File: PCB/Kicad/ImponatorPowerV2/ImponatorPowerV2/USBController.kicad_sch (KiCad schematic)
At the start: 17 parts, among them J3 Conn_01x04_Pin, U1 STUSB4500QTR

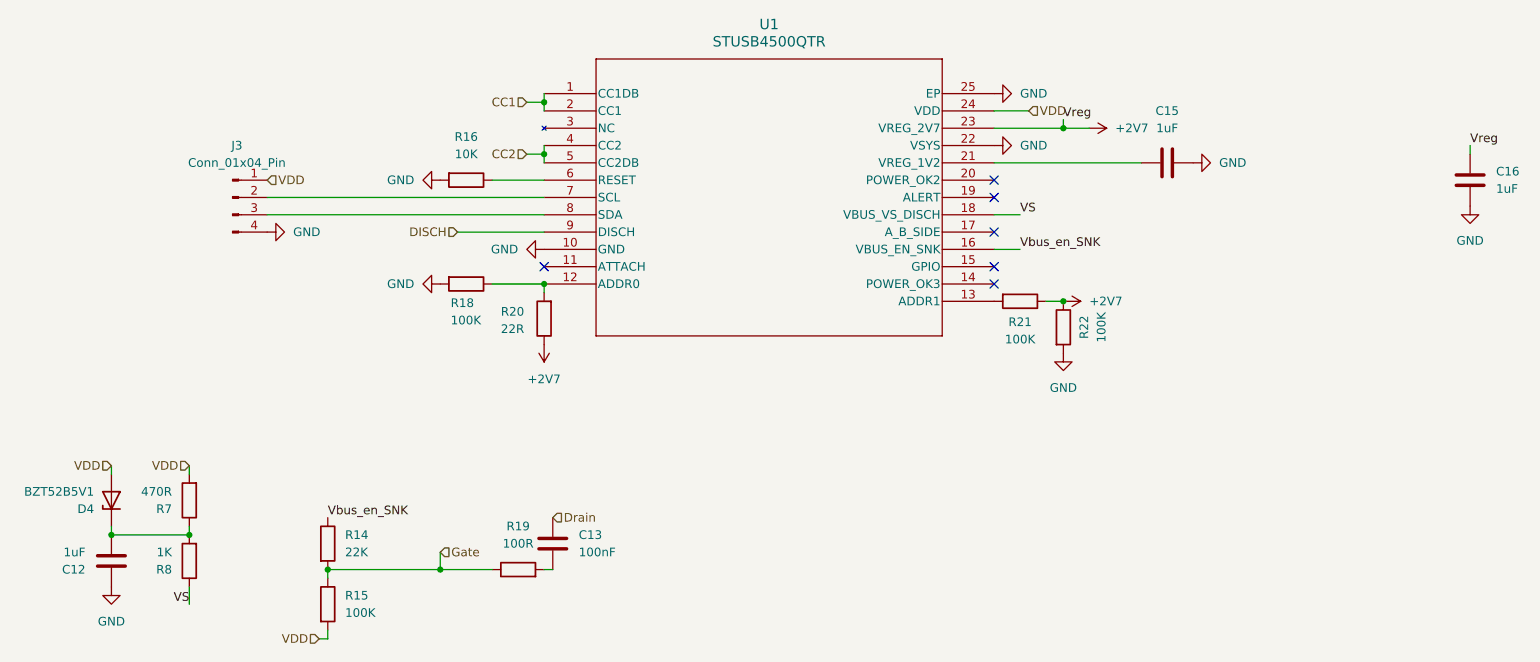
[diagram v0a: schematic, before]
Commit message: PCB routed, not ready for production
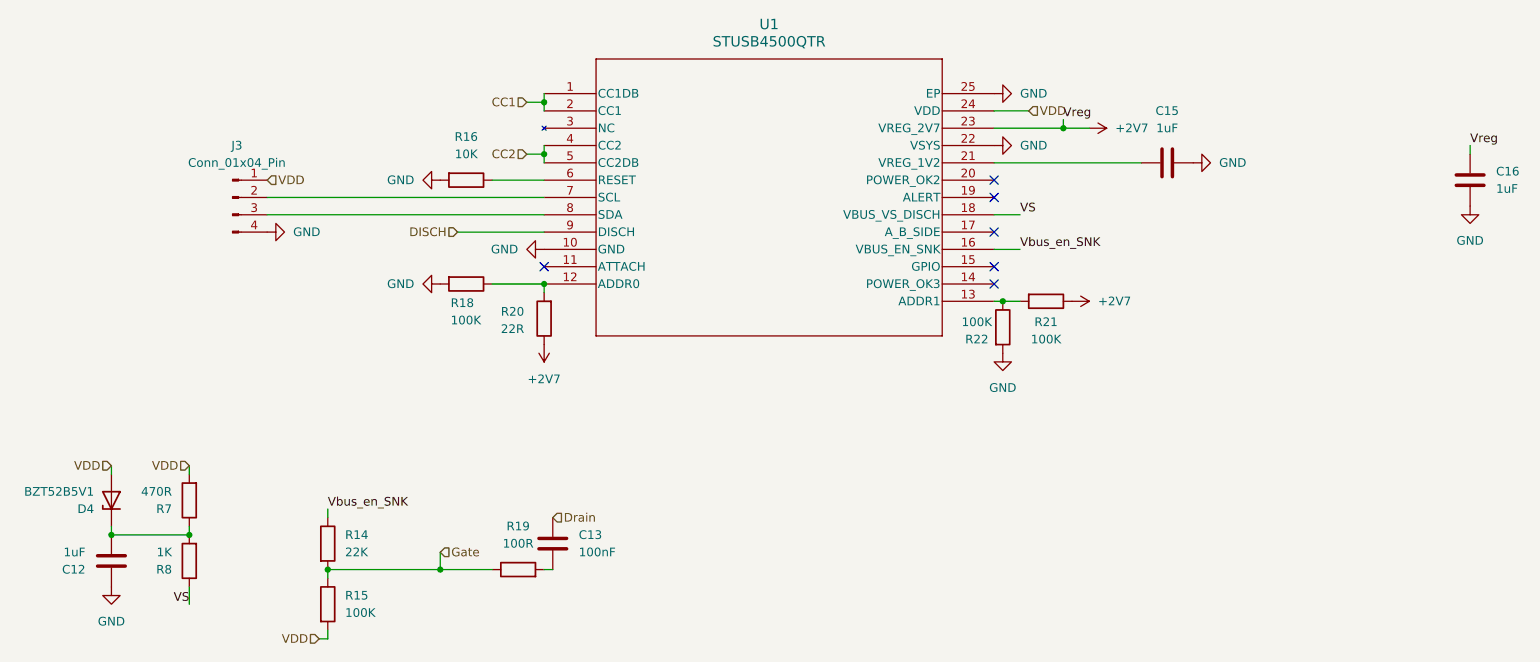
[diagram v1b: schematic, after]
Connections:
- net +2V7: no longer R22.1
- net at R21.2, U1.13 (ADDR1): now also R22.1
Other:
- moved on the sheet: R21, R22
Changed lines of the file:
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@@
 	(paper "A4")
-	(junction
-		(at 179.07 104.14)
-		(diameter 0)
-		(color 0 0 0 0)
-	)
 	(junction
 		(at 102.87 82.55)
@@
 	)
 	(junction
+		(at 170.18 104.14)
+		(diameter 0)
+		(color 0 0 0 0)
+	)
+	(junction
 		(at 102.87 101.6)
 		(diameter 0)
@@
 	(wire
 		(pts
-			(xy 176.53 104.14) (xy 179.07 104.14)
-		)
-		(stroke
-			(width 0)
-			(type default)
-		)
-	)
-	(wire
-		(pts
 			(xy 172.72 96.52) (xy 168.91 96.52)
 		)
@@
 	(wire
 		(pts
+			(xy 71.12 134.62) (xy 71.12 135.89)
+		)
+		(stroke
+			(width 0)
+			(type default)
+		)
+	)
+	(wire
+		(pts
 			(xy 87.63 143.51) (xy 95.25 143.51)
 		)
@@
 	(wire
 		(pts
+			(xy 170.18 104.14) (xy 172.72 104.14)
+		)
+		(stroke
+			(width 0)
+			(type default)
+		)
+	)
+	(wire
+		(pts
 			(xy 102.87 73.66) (xy 102.87 74.93)
 		)
@@
 		(pts
 			(xy 190.5 83.82) (xy 168.91 83.82)
+		)
+		(stroke
+			(width 0)
+			(type default)
+		)
+	)
+	(wire
+		(pts
+			(xy 168.91 104.14) (xy 170.18 104.14)
 		)
 		(stroke
@@
 	)
 	(label "Vbus_en_SNK"
-		(at 71.12 135.89 0)
+		(at 71.12 134.62 0)
 		(effects
 			(font
@@
 	(symbol
 		(lib_id "power:GND")
-		(at 179.07 111.76 0)
+		(at 170.18 111.76 0)
 		(unit 1)
 		(exclude_from_sim no)
@@
 		(fields_autoplaced yes)
 		(property "Reference" "#PWR039"
-			(at 179.07 118.11 0)
+			(at 170.18 118.11 0)
 			(effects
 				(font
@@
 		)
 		(property "Value" "GND"
-			(at 179.07 116.84 0)
+			(at 170.18 116.84 0)
 			(effects
 				(font
@@
 		)
 		(property "Footprint" ""
-			(at 179.07 111.76 0)
+			(at 170.18 111.76 0)
 			(effects
 				(font
@@
 		)
 		(property "Datasheet" ""
-			(at 179.07 111.76 0)
+			(at 170.18 111.76 0)
 			(effects
 				(font
@@
 		)
 		(property "Description" "Power symbol creates a global label with name \"GND\" , ground"
-			(at 179.07 111.76 0)
+			(at 170.18 111.76 0)
 			(effects
 				(font
@@
 	(symbol
 		(lib_id "Device:R")
-		(at 179.07 107.95 0)
+		(at 170.18 107.95 0)
 		(unit 1)
 		(exclude_from_sim no)
@@
 		(dnp no)
 		(property "Reference" "R22"
-			(at 182.118 107.95 90)
+			(at 166.37 109.728 0)
 			(effects
 				(font
@@
 		)
 		(property "Value" "100K"
-			(at 184.658 107.95 90)
+			(at 166.37 107.188 0)
 			(effects
 				(font
@@
 		)
 		(property "Footprint" "Resistor_SMD:R_0603_1608Metric"
-			(at 177.292 107.95 90)
+			(at 168.402 107.95 90)
 			(effects
 				(font
@@
 		)
 		(property "Datasheet" "~"
-			(at 179.07 107.95 0)
+			(at 170.18 107.95 0)
 			(effects
 				(font
@@
 		)
 		(property "Description" "Resistor"
-			(at 179.07 107.95 0)
+			(at 170.18 107.95 0)
 			(effects
 				(font
@@
 	(symbol
 		(lib_id "Device:R")
-		(at 172.72 104.14 270)
+		(at 176.53 104.14 270)
 		(unit 1)
 		(exclude_from_sim no)
@@
 		(dnp no)
 		(property "Reference" "R21"
-			(at 172.72 107.188 90)
+			(at 176.53 107.188 90)
 			(effects
 				(font
@@
 		)
 		(property "Value" "100K"
-			(at 172.72 109.728 90)
+			(at 176.53 109.728 90)
 			(effects
 				(font
@@
 		)
 		(property "Footprint" "Resistor_SMD:R_0603_1608Metric"
-			(at 172.72 102.362 90)
+			(at 176.53 102.362 90)
 			(effects
 				(font
@@
 		)
 		(property "Datasheet" "~"
-			(at 172.72 104.14 0)
+			(at 176.53 104.14 0)
 			(effects
 				(font
@@
 		)
 		(property "Description" "Resistor"
-			(at 172.72 104.14 0)
+			(at 176.53 104.14 0)
 			(effects
 				(font
@@
 	(symbol
 		(lib_id "power:+2V5")
-		(at 179.07 104.14 270)
+		(at 180.34 104.14 270)
 		(unit 1)
 		(exclude_from_sim no)
@@
 		(fields_autoplaced yes)
 		(property "Reference" "#PWR038"
-			(at 175.26 104.14 0)
+			(at 176.53 104.14 0)
 			(effects
 				(font
@@
 		)
 		(property "Value" "+2V7"
-			(at 182.88 104.1399 90)
+			(at 184.15 104.1399 90)
 			(effects
 				(font
@@
 		)
 		(property "Footprint" ""
-			(at 179.07 104.14 0)
+			(at 180.34 104.14 0)
 			(effects
 				(font
@@
 		)
 		(property "Datasheet" ""
-			(at 179.07 104.14 0)
+			(at 180.34 104.14 0)
 			(effects
 				(font
@@
 		)
 		(property "Description" "Power symbol creates a global label with name \"+2V7\""
-			(at 179.07 104.14 0)
-			(effects
-				(font
+			(at 180.34 104.14 0)
+			(effects
+				(font
